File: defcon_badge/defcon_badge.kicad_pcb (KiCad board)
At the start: 4 copper layers, 100 x 160 mm, 79 parts, among them J11 JST-PH 2P, J20 PJ-320A, J30 SAO 2x3, J31 microSD, J32 UART debug, J33 Dev/SWD header, SW1 SS-12D00, SW20 TS-1187A, SW21 TS-1187A, SW22 TS-1187A, U10 TP4056, U11 ME6211C33M5G, U2 W25Q16JVUXIQ, U20 TM8211, U21 TDA1308, U3 RP2040, U30 TSOP4838, Y1 ABM8-272-T3

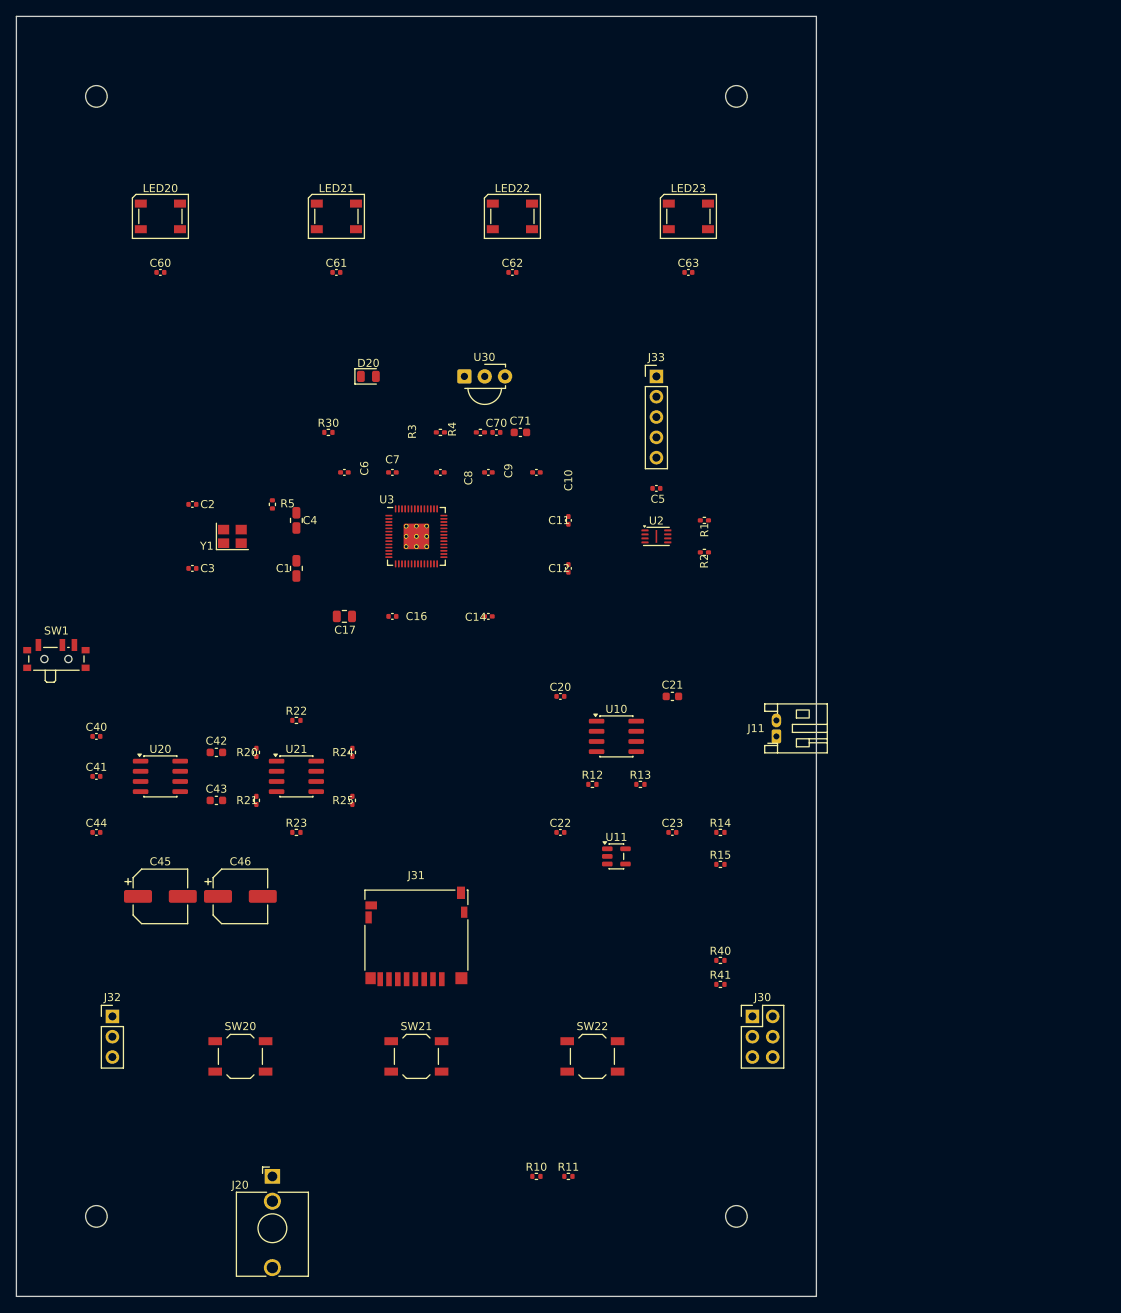
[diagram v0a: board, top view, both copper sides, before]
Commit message: iter(1): set 86x54mm credit-card outline
- tools/set_outline.py applied with --w 86 --h 54 --corner-radius 3
- tools/render_pcb.sh now uses --page-size-mode 1 so components placed
  outside the outline are still visible during iteration
- STATE.md updated; discovered USB-C J10 is present in schematic
  (Connector:USB_C_Receptacle_USB2.0_16P, Connector_USB:USB_C_Receptacle_GCT_USB4085)
  but never transferred to the PCB. Next iter builds a sync tool.

Co-Authored-By: Claude Opus 4.7 (1M context) <noreply@anthropic.com>
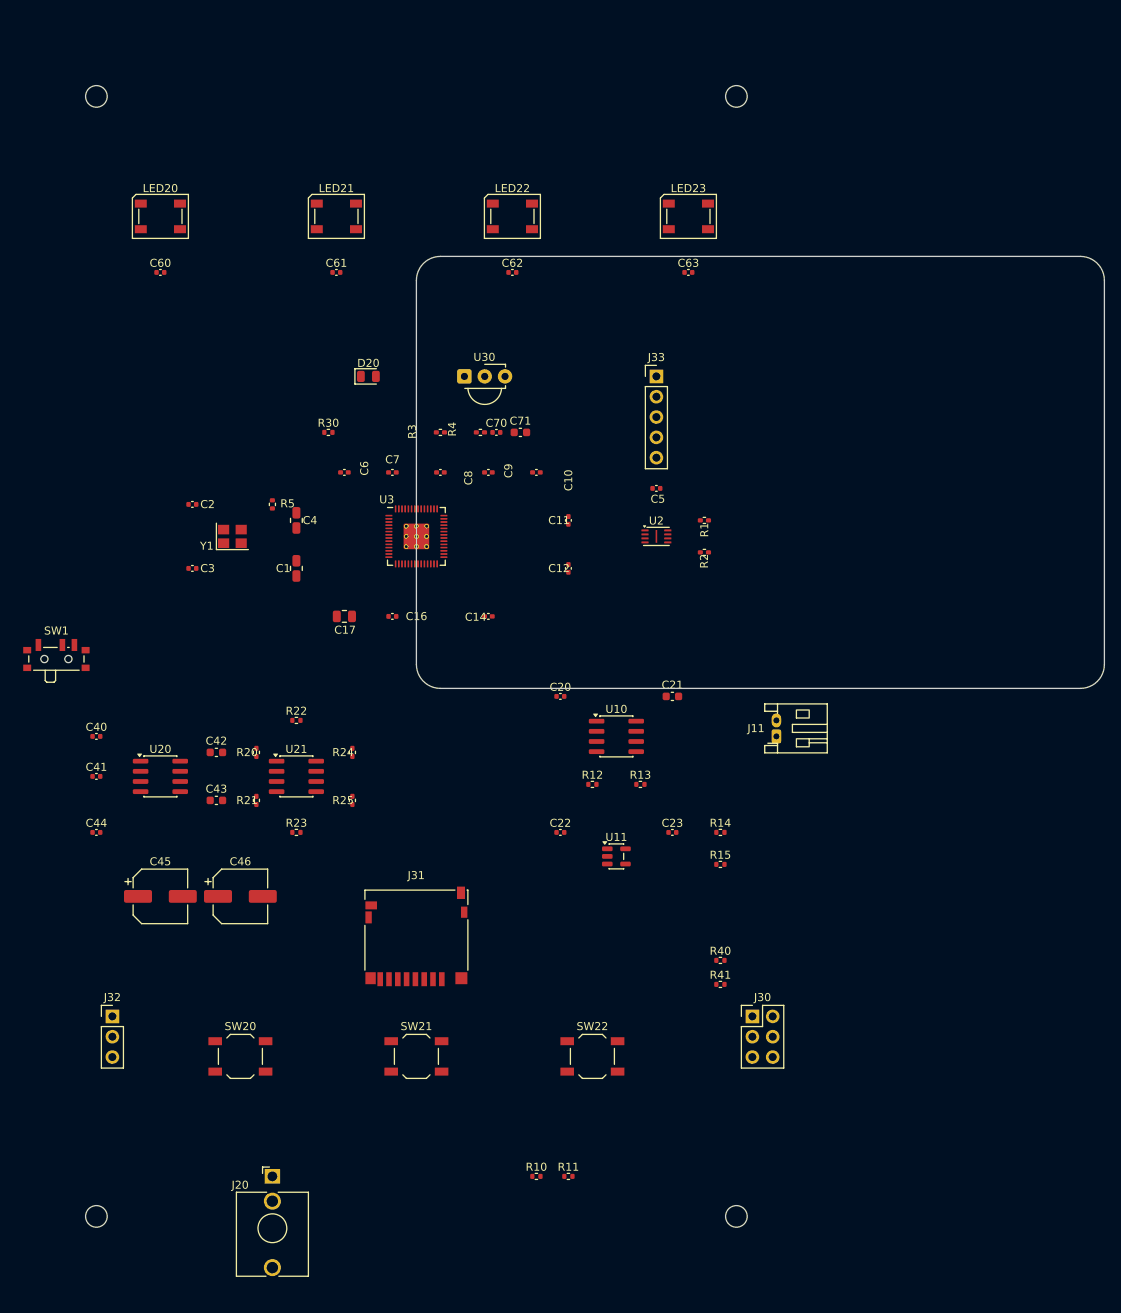
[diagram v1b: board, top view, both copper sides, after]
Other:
- board size 100 x 160 mm -> 86 x 54 mm
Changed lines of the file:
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@@
 	)
 	(embedded_fonts no)
-	(gr_rect (start 50 50) (end 150 210) (stroke (width 0.1) (type solid)) (fill no) (layer "Edge.Cuts"))
+	(gr_line (start 103.000 80.000) (end 183.000 80.000) (stroke (width 0.1) (type default)) (layer "Edge.Cuts"))
+	(gr_line (start 186.000 83.000) (end 186.000 131.000) (stroke (width 0.1) (type default)) (layer "Edge.Cuts"))
+	(gr_line (start 103.000 134.000) (end 183.000 134.000) (stroke (width 0.1) (type default)) (layer "Edge.Cuts"))
+	(gr_line (start 100.000 83.000) (end 100.000 131.000) (stroke (width 0.1) (type default)) (layer "Edge.Cuts"))
+	(gr_arc (start 100.000 83.000) (mid 100.879 80.879) (end 103.000 80.000) (stroke (width 0.1) (type default)) (layer "Edge.Cuts"))
+	(gr_arc (start 183.000 80.000) (mid 185.121 80.879) (end 186.000 83.000) (stroke (width 0.1) (type default)) (layer "Edge.Cuts"))
+	(gr_arc (start 186.000 131.000) (mid 185.121 133.121) (end 183.000 134.000) (stroke (width 0.1) (type default)) (layer "Edge.Cuts"))
+	(gr_arc (start 103.000 134.000) (mid 100.879 133.121) (end 100.000 131.000) (stroke (width 0.1) (type default)) (layer "Edge.Cuts"))
 )

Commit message: iter(2): mounting holes to corners + move_components.py tool
- New tools/move_components.py: generic refdes->position rewriter that
  takes a JSON map (file or stdin) and updates each footprint's anchor
  position + rotation. Will be used for all subsystem placement.
- Used it to move H1-H4 to the corners of the 86x54mm outline with 3mm
  margin: H1=(103,83), H2=(183,83), H3=(103,131), H4=(183,131).
- STATE.md: TODO refined into per-subsystem placement tasks.

Co-Authored-By: Claude Opus 4.7 (1M context) <noreply@anthropic.com>
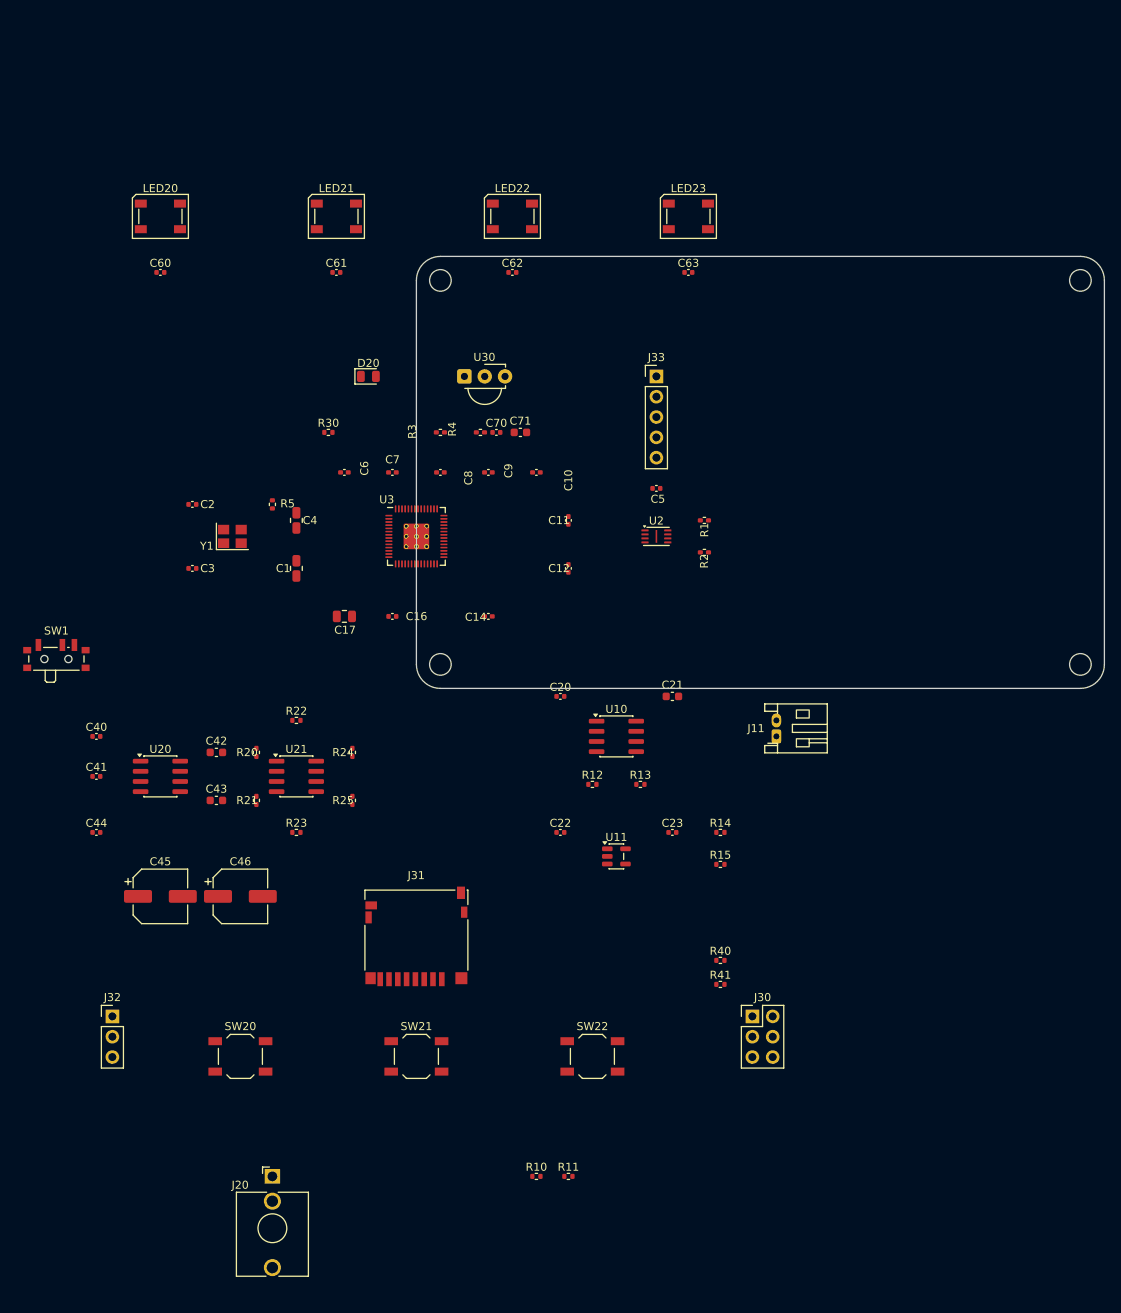
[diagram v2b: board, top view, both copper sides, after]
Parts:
- moved H3 81.3 mm to (103.0, 131.0)
- moved H4 81.3 mm to (183.0, 131.0)
- moved H1 48.8 mm to (103.0, 83.0)
- moved H2 48.8 mm to (183.0, 83.0)
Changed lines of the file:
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@@
 	(footprint "MountingHole:MountingHole_2.7mm_M2.5"
 		(layer "F.Cu")
-		(at 140 60)
+		(at 183.000 83.000)
 		(descr "Mounting Hole 2.7mm, no annular, M2.5")
 		(tags "mounting hole 2.7mm no annular m2.5")
@@
 	(footprint "MountingHole:MountingHole_2.7mm_M2.5"
 		(layer "F.Cu")
-		(at 60 200)
+		(at 103.000 131.000)
 		(descr "Mounting Hole 2.7mm, no annular, M2.5")
 		(tags "mounting hole 2.7mm no annular m2.5")
@@
 	(footprint "MountingHole:MountingHole_2.7mm_M2.5"
 		(layer "F.Cu")
-		(at 60 60)
+		(at 103.000 83.000)
 		(descr "Mounting Hole 2.7mm, no annular, M2.5")
 		(tags "mounting hole 2.7mm no annular m2.5")
@@
 	(footprint "MountingHole:MountingHole_2.7mm_M2.5"
 		(layer "F.Cu")
-		(at 140 200)
+		(at 183.000 131.000)
 		(descr "Mounting Hole 2.7mm, no annular, M2.5")
 		(tags "mounting hole 2.7mm no annular m2.5")

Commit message: iter(3): MCU cluster -> board center
Placed U3 RP2040 at center (143,107) with Y1 crystal + 15p load caps to
its left and U2 W25Q16 flash + R5 boot pull to its right. Tight cluster
~12mm wide centered on the board. Decoupling caps still outside the
outline; iter 4 will bring them in close to U3 power pins.

Co-Authored-By: Claude Opus 4.7 (1M context) <noreply@anthropic.com>
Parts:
- moved R5 67.0 mm to (149.0, 111.0), turned to 0 degrees
- moved C3 65.6 mm to (137.0, 110.0)
- moved C2 65.4 mm to (137.0, 104.0)
- moved Y1 60.5 mm to (137.0, 107.0)
- moved U3 43.7 mm to (143.0, 107.0)
- moved U2 20.6 mm to (149.0, 107.0)
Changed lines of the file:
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@@
 	(footprint "Package_SON:Winbond_USON-8-1EP_3x2mm_P0.5mm_EP0.2x1.6mm"
 		(layer "B.Cu")
-		(at 130 115)
+		(at 149.000 107.000 0)
 		(descr "Winbond  USON, 8 Pin (https://www.lcsc.com/datasheet/lcsc_datasheet_2205122030_Winbond-Elec-W25Q16JVUXIQ_C2843335.pdf#page=66f)")
 		(tags "Winbond USON NoLead")
@@
 	(footprint "RP2040_minimal:RP2040-QFN-56"
 		(layer "B.Cu")
-		(at 100 115)
+		(at 143.000 107.000 0)
 		(descr "QFN, 56 Pin (http://www.cypress.com/file/416486/download#page=40), generated with kicad-footprint-generator ipc_dfn_qfn_generator.py")
 		(tags "QFN DFN_QFN")
@@
 	(footprint "Capacitor_SMD:C_0402_1005Metric"
 		(layer "B.Cu")
-		(at 72 111)
+		(at 137.000 104.000)
 		(descr "Capacitor SMD 0402 (1005 Metric), square (rectangular) end terminal, IPC_7351 nominal, (Body size source: IPC-SM-782 page 76, https://www.pcb-3d.com/wordpress/wp-content/uploads/ipc-sm-782a_amendment_1_and_2.pdf), generated with kicad-footprint-generator")
 		(tags "capacitor")
@@
 	(footprint "Capacitor_SMD:C_0402_1005Metric"
 		(layer "B.Cu")
-		(at 72 119)
+		(at 137.000 110.000)
 		(descr "Capacitor SMD 0402 (1005 Metric), square (rectangular) end terminal, IPC_7351 nominal, (Body size source: IPC-SM-782 page 76, https://www.pcb-3d.com/wordpress/wp-content/uploads/ipc-sm-782a_amendment_1_and_2.pdf), generated with kicad-footprint-generator")
 		(tags "capacitor")
@@
 	(footprint "Crystal:Crystal_SMD_3225-4Pin_3.2x2.5mm"
 		(layer "B.Cu")
-		(at 77 115)
+		(at 137.000 107.000 0)
 		(descr "SMD Crystal SERIES SMD3225/4 http://www.txccrystal.com/images/pdf/7m-accuracy.pdf, 3.2x2.5mm^2 package")
 		(tags "SMD SMT crystal")
@@
 	(footprint "Resistor_SMD:R_0402_1005Metric"
 		(layer "B.Cu")
-		(at 82 111 90)
+		(at 149.000 111.000)
 		(descr "Resistor SMD 0402 (1005 Metric), square (rectangular) end terminal, IPC_7351 nominal, (Body size source: IPC-SM-782 page 72, https://www.pcb-3d.com/wordpress/wp-content/uploads/ipc-sm-782a_amendment_1_and_2.pdf), generated with kicad-footprint-generator")
 		(tags "resistor")
